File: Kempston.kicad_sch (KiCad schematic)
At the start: 19 parts, among them J4 AUDIO, U1 AY-3-8912, U16 74LS138, U18 74LS00, U4 AY-3-8910

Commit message: Added header for AY3-8910 IOB (J18) and moved position of U1 and U4
* Routed AY3-8910 IOB Bits0-7 to header   J18 Pins  1(Bit0)- 8(Bit7)
* AY3-8910 IOA Bits 0-7 can be picked from U1 pins  7(Bit7)-14(Bit0)
* AY3-8912 IOA Bits 1-7 can be picked from U4 Pins 14(Bit7)-20(Bit1)
* AY3-8912 IOA Bit0 can be picked from J20
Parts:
- added J19: AY3_IOB, Connector_PinHeader_2.54mm:PinHeader_1x08_P2.54mm_Vertical, symbol Connector_Generic:Conn_01x08
- added J20: Conn_01x01, Connector_PinHeader_2.54mm:PinHeader_1x01_P2.54mm_Vertical, symbol Connector_Generic:Conn_01x01
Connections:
- net IOB3: now reaches U4.10 (IOB3)
- net IOB3: now also J19.4 (Pin_4)
- net IOB2: now reaches U4.11 (IOB2)
- net IOB2: now also J19.3 (Pin_3)
- net IOB1: now reaches U4.12 (IOB1)
- net IOB1: now also J19.2 (Pin_2)
- net IOB0: now reaches U4.13 (IOB0)
- net IOB0: now also J19.1 (Pin_1)
- net IOA7: now reaches U4.14 (IOA7)
- net IOA7: now also U1.7 (IOA7)
- net IOA6: now reaches U4.15 (IOA6)
- net IOA6: now also U1.8 (IOA6)
- net IOA5: now reaches U4.16 (IOA5)
- net IOA5: now also U1.9 (IOA5)
- net IOA4: now reaches U4.17 (IOA4)
- net IOA4: now also U1.10 (IOA4)
- net IOA3: now reaches U4.18 (IOA3)
- net IOA3: now also U1.11 (IOA3)
- net IOA2: now reaches U4.19 (IOA2)
- net IOA2: now also U1.12 (IOA2)
- net IOA1: now reaches U4.20 (IOA1)
- net IOA1: now also U1.13 (IOA1)
- net IOA0: now reaches U4.21 (IOA0)
- net IOA0: now also U1.14 (IOA0), J20.1 (Pin_1)
- net IOB7: now reaches U4.6 (IOB7)
- net IOB7: now also J19.8 (Pin_8)
- net IOB6: now reaches U4.7 (IOB6)
- net IOB6: now also J19.7 (Pin_7)
- net IOB5: now reaches U4.8 (IOB5)
- net IOB5: now also J19.6 (Pin_6)
- net IOB4: now reaches U4.9 (IOB4)
- net IOB4: now also J19.5 (Pin_5)
- no-connect marks 33 -> 9

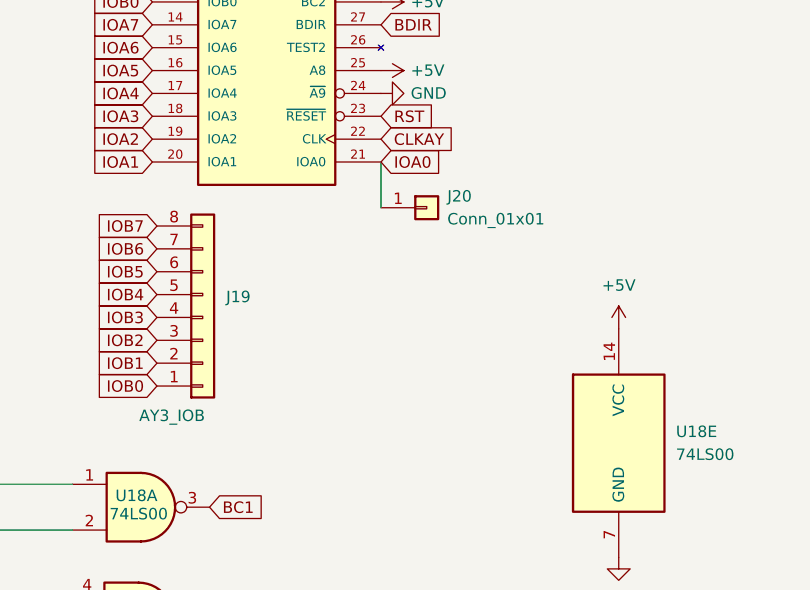
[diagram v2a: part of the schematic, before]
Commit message: Add files via upload
Changed ROM select to 2 pin rather than 3 pin header
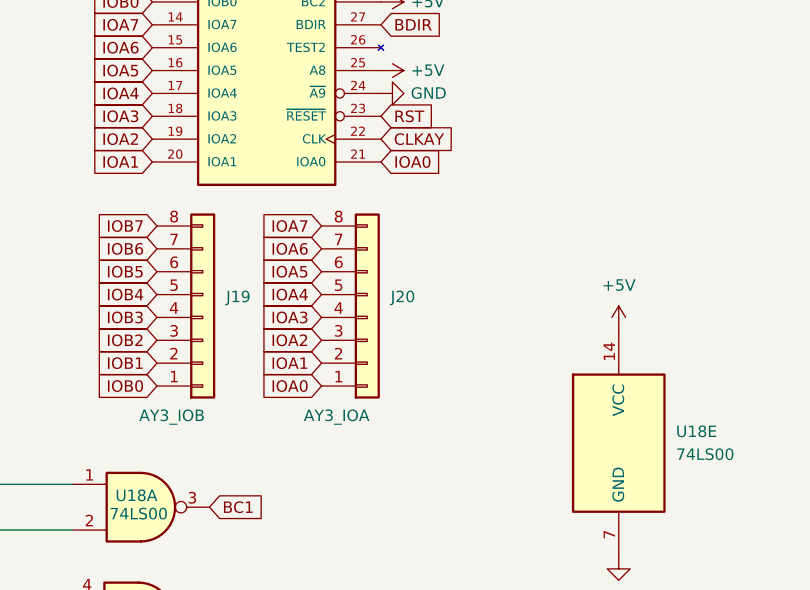
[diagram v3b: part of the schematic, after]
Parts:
- removed J20: Conn_01x01, Connector_PinHeader_2.54mm:PinHeader_1x01_P2.54mm_Vertical, symbol Connector_Generic:Conn_01x01
- added J20: AY3_IOA, Connector_PinHeader_2.54mm:PinHeader_1x08_P2.54mm_Vertical, symbol Connector_Generic:Conn_01x08
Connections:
- net IOA0: now also J20.1 (Pin_1)
- net IOA1: now also J20.2 (Pin_2)
- net IOA2: now also J20.3 (Pin_3)
- net IOA3: now also J20.4 (Pin_4)
- net IOA4: now also J20.5 (Pin_5)
- net IOA5: now also J20.6 (Pin_6)
- net IOA6: now also J20.7 (Pin_7)
- net IOA7: now also J20.8 (Pin_8)
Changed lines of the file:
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@@
-	(wire
-		(pts
-			(xy 149.098 96.774) (xy 149.098 101.854)
-		)
-		(stroke
-			(width 0)
-			(type default)
-		)
-	)
 	(wire
 		(pts
@@
 		)
 	)
+	(global_label "IOA1"
+		(shape input)
+		(at 142.494 119.126 180)
+		(fields_autoplaced yes)
+		(effects
+			(font
+				(size 1.27 1.27)
+			)
+			(justify right)
+		)
+		(property "Intersheetrefs" "${INTERSHEET_REFS}"
+			(at 135.2754 119.126 0)
+			(hide yes)
+			(show_name no)
+			(do_not_autoplace no)
+			(effects
+				(font
+					(size 1.27 1.27)
+				)
+				(justify right)
+			)
+		)
+	)
 	(global_label "RST"
 		(shape input)
@@
 		)
 	)
+	(global_label "IOA4"
+		(shape input)
+		(at 142.494 111.506 180)
+		(fields_autoplaced yes)
+		(effects
+			(font
+				(size 1.27 1.27)
+			)
+			(justify right)
+		)
+		(property "Intersheetrefs" "${INTERSHEET_REFS}"
+			(at 135.2754 111.506 0)
+			(hide yes)
+			(show_name no)
+			(do_not_autoplace no)
+			(effects
+				(font
+					(size 1.27 1.27)
+				)
+				(justify right)
+			)
+		)
+	)
 	(global_label "IOA3"
 		(shape input)
@@
 		)
 	)
+	(global_label "IOA6"
+		(shape input)
+		(at 142.494 106.426 180)
+		(fields_autoplaced yes)
+		(effects
+			(font
+				(size 1.27 1.27)
+			)
+			(justify right)
+		)
+		(property "Intersheetrefs" "${INTERSHEET_REFS}"
+			(at 135.2754 106.426 0)
+			(hide yes)
+			(show_name no)
+			(do_not_autoplace no)
+			(effects
+				(font
+					(size 1.27 1.27)
+				)
+				(justify right)
+			)
+		)
+	)
 	(global_label "D4"
 		(shape input)
@@
 		)
 	)
+	(global_label "IOA0"
+		(shape input)
+		(at 142.494 121.666 180)
+		(fields_autoplaced yes)
+		(effects
+			(font
+				(size 1.27 1.27)
+			)
+			(justify right)
+		)
+		(property "Intersheetrefs" "${INTERSHEET_REFS}"
+			(at 135.2754 121.666 0)
+			(hide yes)
+			(show_name no)
+			(do_not_autoplace no)
+			(effects
+				(font
+					(size 1.27 1.27)
+				)
+				(justify right)
+			)
+		)
+	)
 	(global_label "IOB6"
 		(shape input)
@@
 		)
 	)
+	(global_label "IOA2"
+		(shape input)
+		(at 142.494 116.586 180)
+		(fields_autoplaced yes)
+		(effects
+			(font
+				(size 1.27 1.27)
+			)
+			(justify right)
+		)
+		(property "Intersheetrefs" "${INTERSHEET_REFS}"
+			(at 135.2754 116.586 0)
+			(hide yes)
+			(show_name no)
+			(do_not_autoplace no)
+			(effects
+				(font
+					(size 1.27 1.27)
+				)
+				(justify right)
+			)
+		)
+	)
 	(global_label "D6"
 		(shape input)
@@
 		)
 	)
+	(global_label "IOA5"
+		(shape input)
+		(at 142.494 108.966 180)
+		(fields_autoplaced yes)
+		(effects
+			(font
+				(size 1.27 1.27)
+			)
+			(justify right)
+		)
+		(property "Intersheetrefs" "${INTERSHEET_REFS}"
+			(at 135.2754 108.966 0)
+			(hide yes)
+			(show_name no)
+			(do_not_autoplace no)
+			(effects
+				(font
+					(size 1.27 1.27)
+				)
+				(justify right)
+			)
+		)
+	)
 	(global_label "RD"
 		(shape input)
@@
 		)
 	)
+	(global_label "IOA3"
+		(shape input)
+		(at 142.494 114.046 180)
+		(fields_autoplaced yes)
+		(effects
+			(font
+				(size 1.27 1.27)
+			)
+			(justify right)
+		)
+		(property "Intersheetrefs" "${INTERSHEET_REFS}"
+			(at 135.2754 114.046 0)
+			(hide yes)
+			(show_name no)
+			(do_not_autoplace no)
+			(effects
+				(font
+					(size 1.27 1.27)
+				)
+				(justify right)
+			)
+		)
+	)
 	(global_label "BC1"
 		(shape input)
@@
 		(property "Intersheetrefs" "${INTERSHEET_REFS}"
 			(at 70.7353 94.234 0)
+			(hide yes)
+			(show_name no)
+			(do_not_autoplace no)
+			(effects
+				(font
+					(size 1.27 1.27)
+				)
+				(justify right)
+			)
+		)
+	)
+	(global_label "IOA7"
+		(shape input)
+		(at 142.494 103.886 180)
+		(fields_autoplaced yes)
+		(effects
+			(font
+				(size 1.27 1.27)
+			)
+			(justify right)
+		)
+		(property "Intersheetrefs" "${INTERSHEET_REFS}"
+			(at 135.2754 103.886 0)
 			(hide yes)
 			(show_name no)
@@
 	)
 	(symbol
+		(lib_id "Connector_Generic:Conn_01x08")
+		(at 147.574 114.046 0)
+		(mirror x)
+		(unit 1)
+		(body_style 1)
+		(exclude_from_sim no)
+		(in_bom yes)
+		(on_board yes)
+		(in_pos_files yes)
+		(dnp no)
+		(property "Reference" "J20"
+			(at 152.908 111.76 0)
+			(show_name no)
+			(do_not_autoplace no)
+			(effects
+				(font
+					(size 1.27 1.27)
+				)
+				(justify right)
+			)
+		)
+		(property "Value" "AY3_IOA"
+			(at 147.828 124.968 0)
+			(show_name no)
+			(do_not_autoplace no)
+			(effects
+				(font
+					(size 1.27 1.27)
+				)
+				(justify right)
+			)
+		)
+		(property "Footprint" "Connector_PinHeader_2.54mm:PinHeader_1x08_P2.54mm_Vertical"
+			(at 147.574 114.046 0)
+			(hide yes)
+			(show_name no)
+			(do_not_autoplace no)
+			(effects
+				(font
+					(size 1.27 1.27)
+				)
+			)
+		)
+		(property "Datasheet" ""
+			(at 147.574 114.046 0)
+			(hide yes)
+			(show_name no)
+			(do_not_autoplace no)
+			(effects
+				(font
+					(size 1.27 1.27)
+				)
+			)
+		)
+		(property "Description" "Generic connector, single row, 01x02, script generated (kicad-library-utils/schlib/autogen/connector/)"
+			(at 147.574 114.046 0)
+			(hide yes)
+			(show_name no)
+			(do_not_autoplace no)
+			(effects
+				(font
+					(size 1.27 1.27)
+				)
+			)
+		)
+		(pin "1"
+		)
+		(pin "2"
+		)
+		(pin "3"
+		)
+		(pin "4"
+		)
+		(pin "8"
+		)
+		(pin "7"
+		)
+		(pin "6"
+		)
+		(pin "5"
+		)
+		(instances
+			(project "ZXSpider48"
+				(path "/c8dee8da-cc77-415a-9e31-9e236c26c0e6/784c5548-3888-4820-9f8e-441c9fec3986"
+					(reference "J20")
+					(unit 1)
+				)
+			)
+		)
+	)
+	(symbol
 		(lib_id "Device:R")
 		(at 195.58 71.12 270)
@@
 					(unit 1)
 				)
-			)
-		)
-	)
-	(symbol
-		(lib_id "Connector_Generic:Conn_01x01")
-		(at 154.178 101.854 0)
-		(unit 1)
-		(body_style 1)
-		(exclude_from_sim no)
-		(in_bom yes)
-		(on_board yes)
-		(in_pos_files yes)
-		(dnp no)
-		(fields_autoplaced yes)
-		(property "Reference" "J20"
-			(at 156.464 100.5839 0)
-			(show_name no)
-			(do_not_autoplace no)
-			(effects
-				(font
-					(size 1.27 1.27)
-				)
-				(justify left)
-			)
-		)
-		(property "Value" "Conn_01x01"
-			(at 156.464 103.1239 0)
-			(show_name no)
-			(do_not_autoplace no)
-			(effects
-				(font
-					(size 1.27 1.27)
-				)
-				(justify left)
-			)
-		)
-		(property "Footprint" "Connector_PinHeader_2.54mm:PinHeader_1x01_P2.54mm_Vertical"
-			(at 154.178 101.854 0)
-			(hide yes)
-			(show_name no)
-			(do_not_autoplace no)
-			(effects
-				(font
-					(size 1.27 1.27)
-				)
-			)
-		)
-		(property "Datasheet" ""
-			(at 154.178 101.854 0)
-			(hide yes)
-			(show_name no)
-			(do_not_autoplace no)
-			(effects
-				(font
-					(size 1.27 1.27)
-				)
-			)
-		)
-		(property "Description" "Generic connector, single row, 01x01, script generated (kicad-library-utils/schlib/autogen/connector/)"
-			(at 154.178 101.854 0)
-			(hide yes)
-			(show_name no)
-			(do_not_autoplace no)
-			(effects
-				(font
-					(size 1.27 1.27)
-				)
-			)
-		)
-		(pin "1"
-		)
-		(instances
-			(project "ZXSpider48"
-				(path "/c8dee8da-cc77-415a-9e31-9e236c26c0e6/784c5548-3888-4820-9f8e-441c9fec3986"
-					(reference "J20")
-					(unit 1)
-				)
